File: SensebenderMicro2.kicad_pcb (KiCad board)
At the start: 2 copper layers, 21.5 x 32 mm, 50 parts, among them P2 MYSX_2.4, P3 Antenna, Q1 SI2333DDS-T1-GE3, U1 ATSAMD21E, U2 MCP1703T-3302E, U3 NRF24L01, U4 RFM69HW, U5 ATSHA204A, U6 AT45DB041E, U7 Si7021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

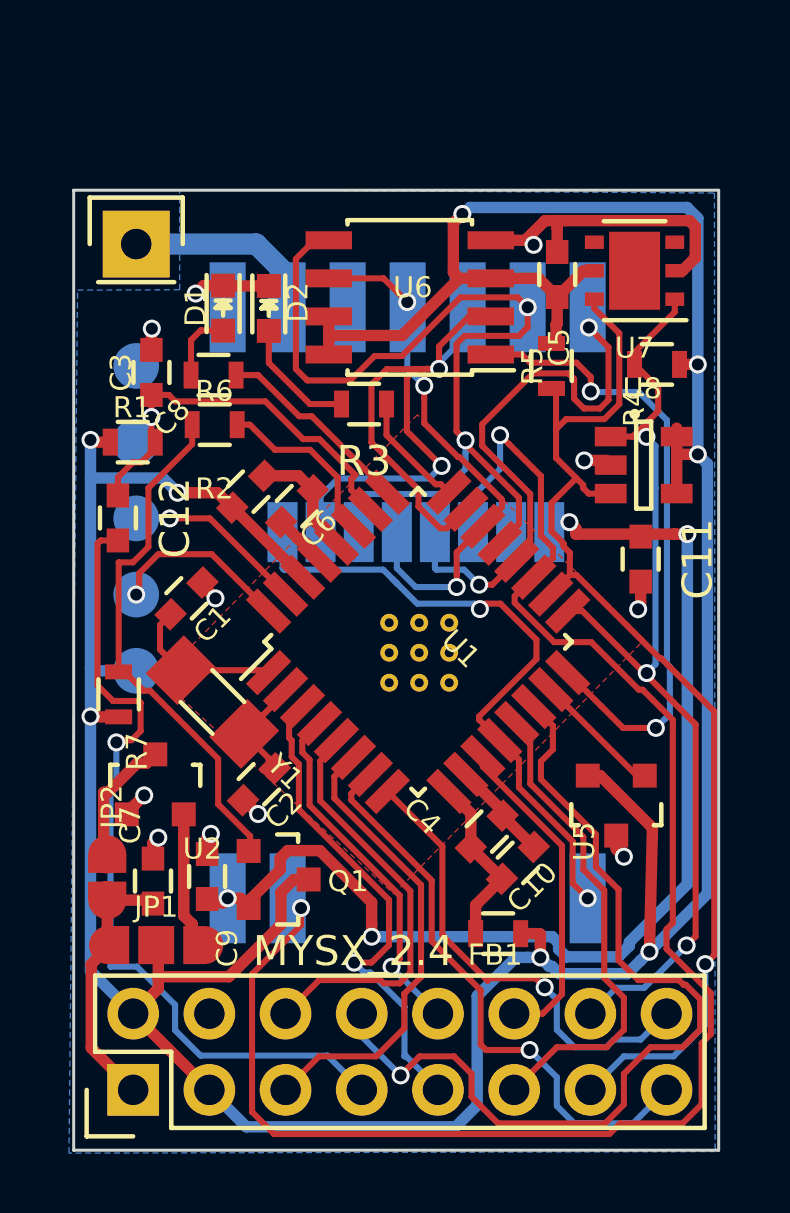
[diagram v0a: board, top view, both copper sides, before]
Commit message: Updated routing, waveguide for rfm69
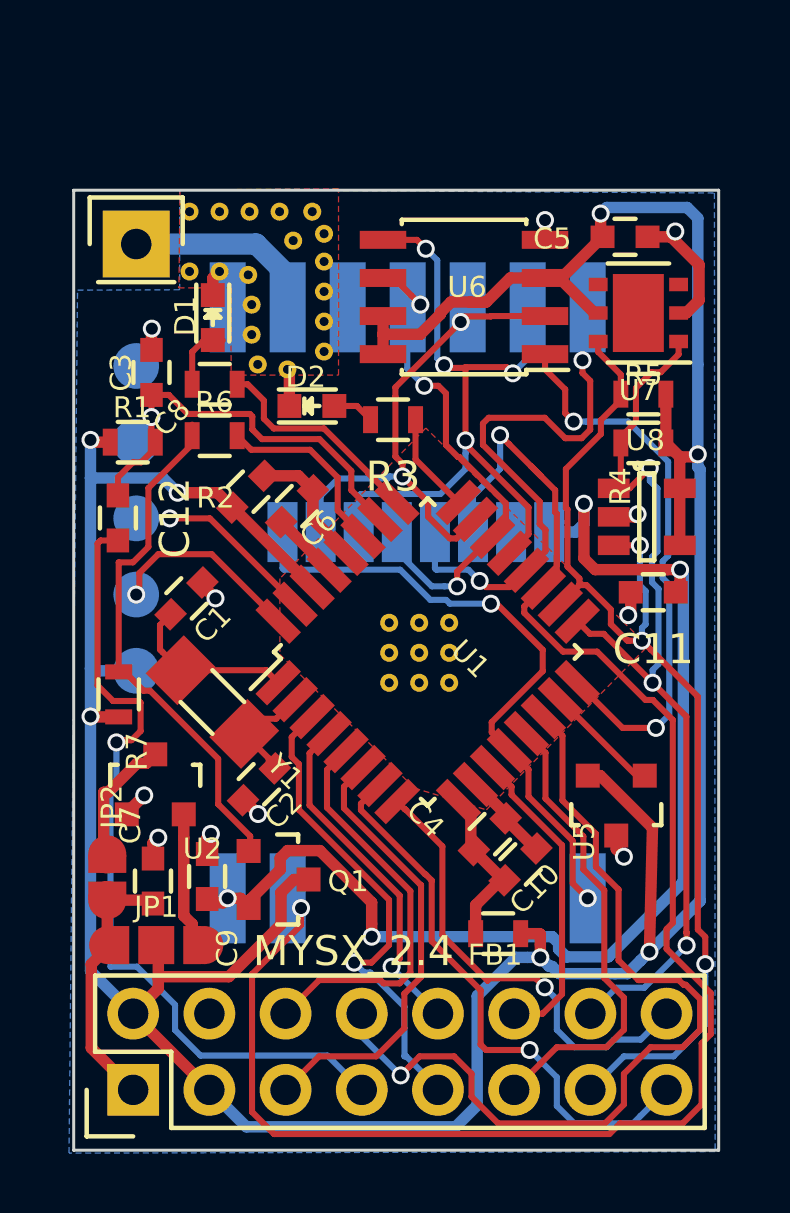
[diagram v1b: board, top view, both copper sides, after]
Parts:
- added REF**: via-0.6mm, mysensors_obscurities:via-0.6mm, F.Cu at (97.3, 83.5)
- added REF**: via-0.6mm, mysensors_obscurities:via-0.6mm, F.Cu at (96.1, 88.0)
- added REF**: via-0.6mm, mysensors_obscurities:via-0.6mm, F.Cu at (96.3, 83.7)
- added REF**: via-0.6mm, mysensors_obscurities:via-0.6mm, F.Cu at (94.8, 84.8)
- added REF**: via-0.6mm, mysensors_obscurities:via-0.6mm, F.Cu at (93.9, 84.7)
- added REF**: via-0.6mm, mysensors_obscurities:via-0.6mm, F.Cu at (92.9, 84.7)
- added REF**: via-0.6mm, mysensors_obscurities:via-0.6mm, F.Cu at (95.9, 82.7)
- added REF**: via-0.6mm, mysensors_obscurities:via-0.6mm, F.Cu at (94.9, 82.7)
- added REF**: via-0.6mm, mysensors_obscurities:via-0.6mm, F.Cu at (93.9, 82.7)
- added REF**: via-0.6mm, mysensors_obscurities:via-0.6mm, F.Cu at (92.9, 82.7)
- added REF**: via-0.6mm, mysensors_obscurities:via-0.6mm, F.Cu at (95.1, 87.8)
- added REF**: via-0.6mm, mysensors_obscurities:via-0.6mm, F.Cu at (94.9, 86.8)
- added REF**: via-0.6mm, mysensors_obscurities:via-0.6mm, F.Cu at (94.9, 85.8)
- added REF**: via-0.6mm, mysensors_obscurities:via-0.6mm, F.Cu at (97.3, 87.4)
- added REF**: via-0.6mm, mysensors_obscurities:via-0.6mm, F.Cu at (97.3, 86.4)
- added REF**: via-0.6mm, mysensors_obscurities:via-0.6mm, F.Cu at (97.3, 85.4)
- added REF**: via-0.6mm, mysensors_obscurities:via-0.6mm, F.Cu at (97.3, 84.4)
- added REF**: via-0.6mm, mysensors_obscurities:via-0.6mm, F.Cu at (97.0, 82.7)
- moved D2 3.55 mm to (96.9, 89.2), turned to 0 degrees
- moved R5 3.20 mm to (108.0, 88.8), turned to 180 degrees
- moved R4 2.66 mm to (108.0, 90.4)
- moved C5 2.59 mm to (107.4, 83.6), turned to 180 degrees
- moved U6 1.81 mm to (102.0, 85.6)
- moved U8 1.73 mm to (108.1, 92.9)
- moved U7 1.42 mm to (107.8, 86.1)
- moved C11 1.18 mm to (108.3, 95.4), turned to 180 degrees
- moved R3 1.10 mm to (99.6, 89.6)
- moved D1 0.47 mm to (93.6, 86.2)
- moved U1 0.46 mm to (100.8, 97.4)
- moved R6 0.37 mm to (93.7, 90.2)
- moved R2 0.31 mm to (93.7, 88.5)
- moved C4 0.14 mm to (102.9, 103.5)
- moved C10 0.10 mm to (103.9, 104.5)
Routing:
- net /MISO: track 25.2 -> 17.3 mm
- net /MOSI: track 31.3 -> 23.9 mm, vias 2 -> 4
- net GND: track 27.6 -> 21.4 mm
- net +3V3: track 125.9 -> 120.8 mm, vias 8 -> 7
- net Net-(D2-Pad2): track 4.06 -> 1.40 mm
- net /FLS_CS: track 21.2 -> 18.8 mm
- net +3.3VP: track 37.6 -> 39.6 mm
- net /D7_SCL: track 37.7 -> 36.0 mm, vias 1 -> 3
- net /SCK: track 17.9 -> 16.5 mm
- net /D8_SDA: track 32.7 -> 31.7 mm
- net /LEGACY_ID: track 30.3 -> 29.5 mm
- net /CSN: track 19.2 -> 19.8 mm
- net Net-(R3-Pad1): track 3.90 -> 3.35 mm
- net /NRF_CE_RFM_DIO5: track 54.8 -> 55.3 mm

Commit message: Updated routing, gnd on component side
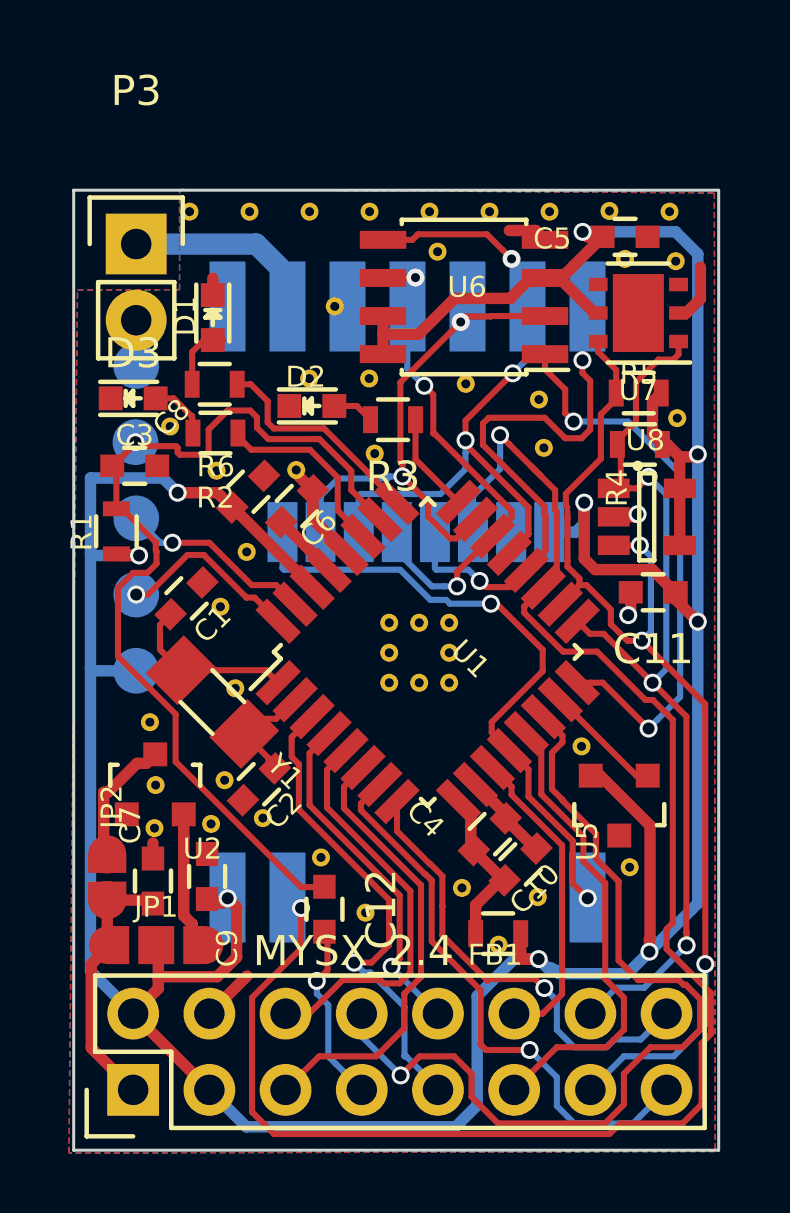
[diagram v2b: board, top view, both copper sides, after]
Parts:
- removed Q1: SI2333DDS-T1-GE3, TO_SOT_Packages_SMD:SOT-23
- removed R7: 100K, Resistors_SMD:R_0603
- removed the REF** at (97.3, 83.5)
- removed the REF** at (96.1, 88.0)
- removed the REF** at (96.3, 83.7)
- removed the REF** at (94.8, 84.8)
- removed the REF** at (93.9, 84.7)
- removed the REF** at (92.9, 84.7)
- removed the REF** at (95.9, 82.7)
- removed the REF** at (93.9, 82.7)
- removed the REF** at (95.1, 87.8)
- removed the REF** at (100.5, 97.4)
- removed the REF** at (94.9, 86.8)
- removed the REF** at (94.9, 85.8)
- removed the REF** at (97.3, 87.4)
- removed the REF** at (97.3, 86.4)
- removed the REF** at (97.3, 85.4)
- removed the REF** at (97.3, 84.4)
- removed the REF** at (97.0, 82.7)
- added D3: LED, LEDs:LED-0603, F.Cu at (91.0, 88.9)
- added REF**: via-0.6mm, mysensors_obscurities:via-0.6mm, F.Cu at (94.0, 101.7)
- added REF**: via-0.6mm, mysensors_obscurities:via-0.6mm, F.Cu at (98.7, 106.1)
- added REF**: via-0.6mm, mysensors_obscurities:via-0.6mm, F.Cu at (91.5, 99.7)
- added REF**: via-0.6mm, mysensors_obscurities:via-0.6mm, F.Cu at (95.3, 102.9)
- added REF**: via-0.6mm, mysensors_obscurities:via-0.6mm, F.Cu at (94.8, 94.1)
- added REF**: via-0.6mm, mysensors_obscurities:via-0.6mm, F.Cu at (93.9, 95.9)
- added REF**: via-0.6mm, mysensors_obscurities:via-0.6mm, F.Cu at (101.1, 84.0)
- added REF**: via-0.6mm, mysensors_obscurities:via-0.6mm, F.Cu at (94.4, 98.6)
- added REF**: via-0.6mm, mysensors_obscurities:via-0.6mm, F.Cu at (109.1, 89.6)
- added REF**: via-0.6mm, mysensors_obscurities:via-0.6mm, F.Cu at (109.1, 84.4)
- added REF**: via-0.6mm, mysensors_obscurities:via-0.6mm, F.Cu at (99.0, 90.8)
- added REF**: via-0.6mm, mysensors_obscurities:via-0.6mm, F.Cu at (93.6, 103.1)
- added REF**: via-0.6mm, mysensors_obscurities:via-0.6mm, F.Cu at (104.7, 90.6)
- added REF**: via-0.6mm, mysensors_obscurities:via-0.6mm, F.Cu at (104.5, 89.0)
- added REF**: via-0.6mm, mysensors_obscurities:via-0.6mm, F.Cu at (102.1, 88.5)
- added REF**: via-0.6mm, mysensors_obscurities:via-0.6mm, F.Cu at (93.8, 91.4)
- added REF**: via-0.6mm, mysensors_obscurities:via-0.6mm, F.Cu at (96.4, 91.3)
- added REF**: via-0.6mm, mysensors_obscurities:via-0.6mm, F.Cu at (92.2, 89.9)
- added REF**: via-0.6mm, mysensors_obscurities:via-0.6mm, F.Cu at (91.7, 103.3)
- added REF**: via-0.6mm, mysensors_obscurities:via-0.6mm, F.Cu at (91.7, 101.8)
- added REF**: via-0.6mm, mysensors_obscurities:via-0.6mm, F.Cu at (97.2, 104.2)
- added REF**: via-0.6mm, mysensors_obscurities:via-0.6mm, F.Cu at (103.2, 107.1)
- added REF**: via-0.6mm, mysensors_obscurities:via-0.6mm, F.Cu at (107.5, 104.6)
- added REF**: via-0.6mm, mysensors_obscurities:via-0.6mm, F.Cu at (104.5, 105.6)
- added REF**: via-0.6mm, mysensors_obscurities:via-0.6mm, F.Cu at (98.9, 88.3)
- added REF**: via-0.6mm, mysensors_obscurities:via-0.6mm, F.Cu at (96.9, 88.3)
- added REF**: via-0.6mm, mysensors_obscurities:via-0.6mm, F.Cu at (104.9, 82.7)
- added REF**: via-0.6mm, mysensors_obscurities:via-0.6mm, F.Cu at (102.9, 82.7)
- added REF**: via-0.6mm, mysensors_obscurities:via-0.6mm, F.Cu at (100.9, 82.7)
- added REF**: via-0.6mm, mysensors_obscurities:via-0.6mm, F.Cu at (98.9, 82.7)
- added REF**: via-0.6mm, mysensors_obscurities:via-0.6mm, F.Cu at (96.9, 82.7)
- added REF**: via-0.6mm, mysensors_obscurities:via-0.6mm, F.Cu at (105.9, 100.5)
- added REF**: via-0.6mm, mysensors_obscurities:via-0.6mm, F.Cu at (97.7, 85.9)
- added REF**: via-0.6mm, mysensors_obscurities:via-0.6mm, F.Cu at (108.9, 82.7)
- added REF**: via-0.6mm, mysensors_obscurities:via-0.6mm, F.Cu at (106.9, 82.7)
- added REF**: via-0.6mm, mysensors_obscurities:via-0.6mm, F.Cu at (107.4, 84.3)
- added REF**: via-0.6mm, mysensors_obscurities:via-0.6mm, F.Cu at (101.9, 105.3)
- P3: footprint Pin_Headers:Pin_Header_Straight_1x01 -> Pin_Headers:Pin_Header_Straight_1x02
- R6: value 100R -> 220R
- moved C12 14.7 mm to (97.4, 106.0)
- moved C3 3.16 mm to (91.0, 91.2), turned to 0 degrees
- moved R1 3.02 mm to (90.4, 93.4), turned to 90 degrees
- moved R5 0.16 mm to (107.8, 88.8)
- moved R4 0.13 mm to (107.9, 90.5)
- moved U5 0.10 mm to (107.2, 102.5)
- moved R6 0.09 mm to (93.7, 90.1), turned to 180 degrees
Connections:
- C11 pad 1: +3.3VP -> +3V3
- C9 pad 2: +3.3VP -> +3V3
- R6 pad 1: Net-(Q1-Pad1) -> Net-(R6-Pad1)
- R6 pad 2: Net-(R6-Pad2) -> Net-(D3-Pad2)
- U1 pad 27: Net-(R6-Pad2) -> Net-(R6-Pad1)
- U3 pad 2: +3.3VP -> +3V3
- U4 pad 8: +3.3VP -> +3V3
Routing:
- net +3.3VP: track 39.6 -> 0.00 mm, vias 4 -> 0
- net /RST: track 27.2 -> 6.03 mm
- net Net-(Q1-Pad1): track 17.6 -> 0.00 mm
- net /RESET: track 14.6 -> 31.5 mm
- net +3V3: track 120.8 -> 128.1 mm, vias 7 -> 9
- net GND: track 21.4 -> 14.3 mm, vias 11 -> 2
- net Net-(R6-Pad2): track 5.77 -> 0.00 mm
- net Net-(R6-Pad1): track 0.00 -> 5.77 mm
- net Net-(D3-Pad2): track 0.00 -> 2.12 mm
- net /MOSI: track 23.9 -> 22.8 mm, vias 4 -> 3
- net /SCK: track 16.5 -> 15.9 mm

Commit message: Updates to layout, copper pour etc
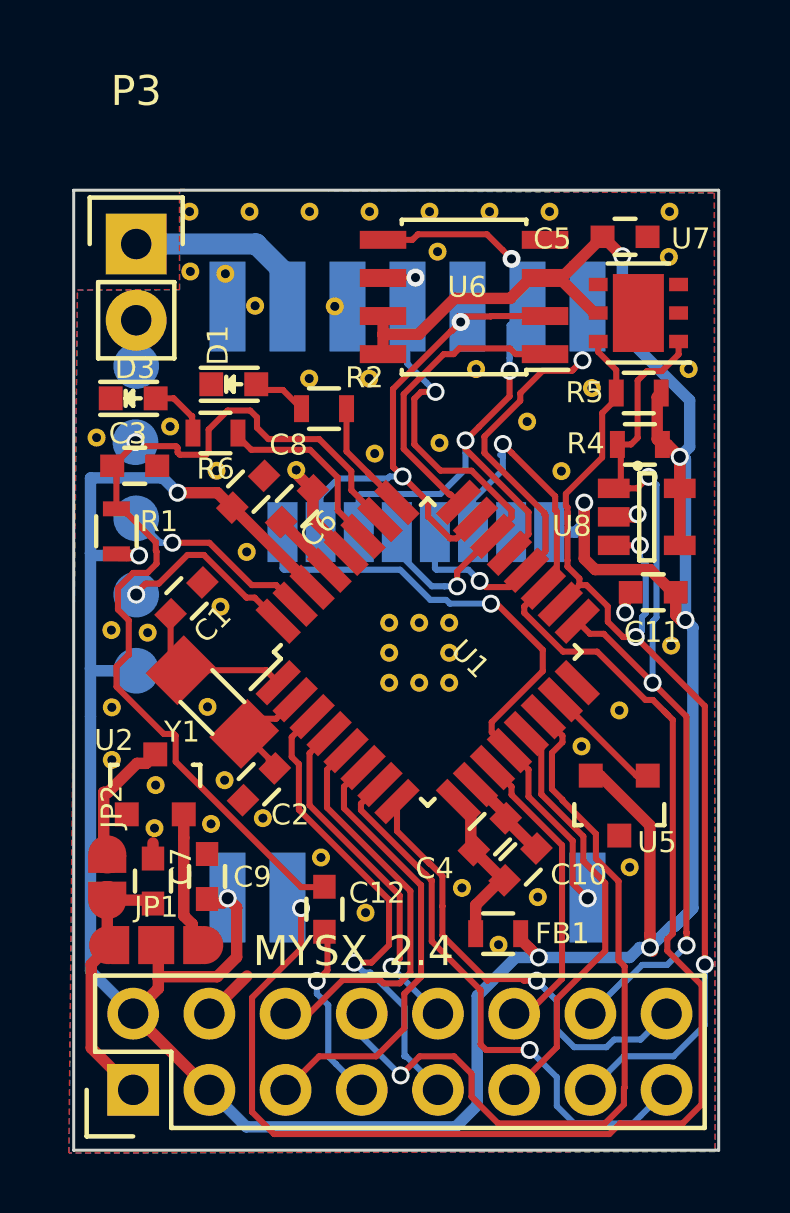
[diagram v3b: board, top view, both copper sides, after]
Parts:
- removed D2: LED, LEDs:LED-0603
- removed R3: 220R, Resistors_SMD:R_0603
- removed the REF** at (91.5, 99.7)
- removed the REF** at (109.1, 89.6)
- removed the REF** at (109.1, 84.4)
- removed the REF** at (102.1, 88.5)
- removed the REF** at (106.9, 82.7)
- removed the REF** at (107.4, 84.3)
- added REF**: via-0.6mm, mysensors_obscurities:via-0.6mm, F.Cu at (101.2, 90.4)
- added REF**: via-0.6mm, mysensors_obscurities:via-0.6mm, F.Cu at (90.3, 99.2)
- added REF**: via-0.6mm, mysensors_obscurities:via-0.6mm, F.Cu at (108.9, 97.2)
- added REF**: via-0.6mm, mysensors_obscurities:via-0.6mm, F.Cu at (89.8, 90.2)
- added REF**: via-0.6mm, mysensors_obscurities:via-0.6mm, F.Cu at (90.3, 101.0)
- added REF**: via-0.6mm, mysensors_obscurities:via-0.6mm, F.Cu at (91.5, 96.7)
- added REF**: via-0.6mm, mysensors_obscurities:via-0.6mm, F.Cu at (90.3, 96.7)
- added REF**: via-0.6mm, mysensors_obscurities:via-0.6mm, F.Cu at (102.4, 88.0)
- added REF**: via-0.6mm, mysensors_obscurities:via-0.6mm, F.Cu at (107.2, 99.3)
- added REF**: via-0.6mm, mysensors_obscurities:via-0.6mm, F.Cu at (92.9, 84.7)
- added REF**: via-0.6mm, mysensors_obscurities:via-0.6mm, F.Cu at (94.1, 84.8)
- added REF**: via-0.6mm, mysensors_obscurities:via-0.6mm, F.Cu at (95.0, 85.9)
- added REF**: via-0.6mm, mysensors_obscurities:via-0.6mm, F.Cu at (108.8, 84.2)
- added REF**: via-0.6mm, mysensors_obscurities:via-0.6mm, F.Cu at (109.5, 88.0)
- added REF**: via-0.6mm, mysensors_obscurities:via-0.6mm, F.Cu at (105.3, 91.4)
- moved R2 3.73 mm to (97.3, 89.3)
- moved D1 2.33 mm to (94.3, 88.5), turned to 0 degrees
- moved REF** 1.81 mm to (106.3, 88.6)
- moved REF** 1.11 mm to (93.5, 99.2)
- moved REF** 1.04 mm to (104.1, 89.7)
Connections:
- U1 pad 16: /FLS_CS -> Net-(U1-Pad16)
- U1 pad 24: Net-(R3-Pad1) -> /FLS_CS
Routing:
- net /FLS_CS: track 18.9 -> 9.81 mm, vias 2 -> 0
- net GND: track 14.3 -> 10.3 mm
- net +3V3: track 128.1 -> 124.5 mm
- net /LEGACY_ID: track 29.8 -> 26.3 mm
- net Net-(R2-Pad1): track 6.92 -> 3.52 mm
- net Net-(R3-Pad1): track 3.35 -> 0.00 mm
- net /CSN: track 19.8 -> 17.4 mm
- net /D5_PWM: track 15.7 -> 14.2 mm
- net /SCK: track 15.9 -> 17.3 mm
- net Net-(D2-Pad2): track 1.40 -> 0.00 mm
- net /NRF_CE_RFM_DIO5: track 55.2 -> 54.1 mm
- net /RESET: track 31.5 -> 32.1 mm

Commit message: Added extra 10uF caps to radios
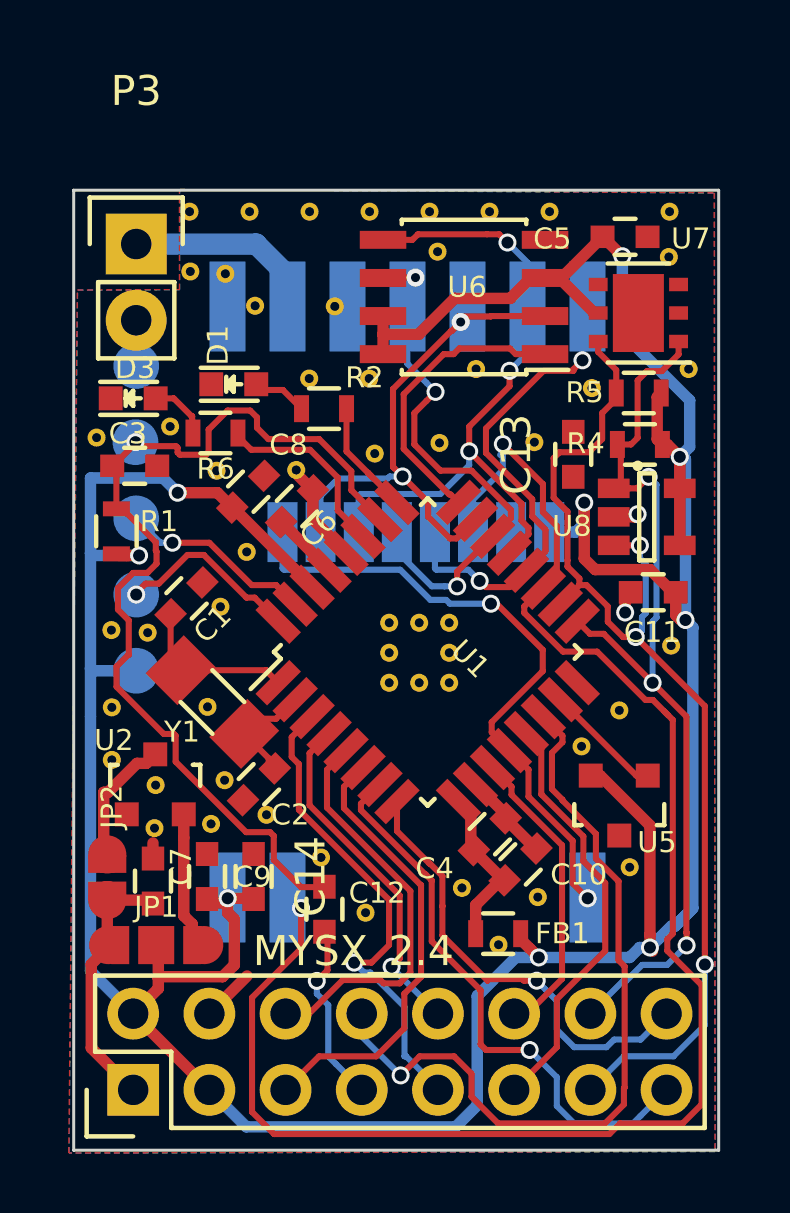
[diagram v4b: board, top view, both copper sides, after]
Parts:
- removed the REF** at (105.3, 91.4)
- added C13: 100nF, Capacitors_SMD:C_0603, F.Cu at (105.7, 90.8)
- added C14: 10uF, Capacitors_SMD:C_0603, F.Cu at (95.0, 104.9)
- C11: value 4,7uF -> 10uF
- moved REF** 0.73 mm to (104.4, 90.4)
- moved REF** 0.17 mm to (95.4, 102.8)
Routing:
- net /MOSI: track 22.8 -> 24.0 mm
- net +3V3: track 124.5 -> 125.4 mm
- net /D7_SCL: track 36.0 -> 36.7 mm
